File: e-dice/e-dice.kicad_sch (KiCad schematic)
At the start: 49 parts, among them J1 mid_conn_1, J2 top_conn_1, J3 mid_conn_2, J4 top_conn_2, J6 bot_conn_1, J7 bot_conn_2, J8 mid_conn_3, J9 mid_conn_4, Q1 2N3904, Q2 2N3904, Q3 2N3904, Q4 2N3906, Q5 2N3904, Q6 2N3904, Q7 2N3904, SW1 SW_SPDT, U1 4017

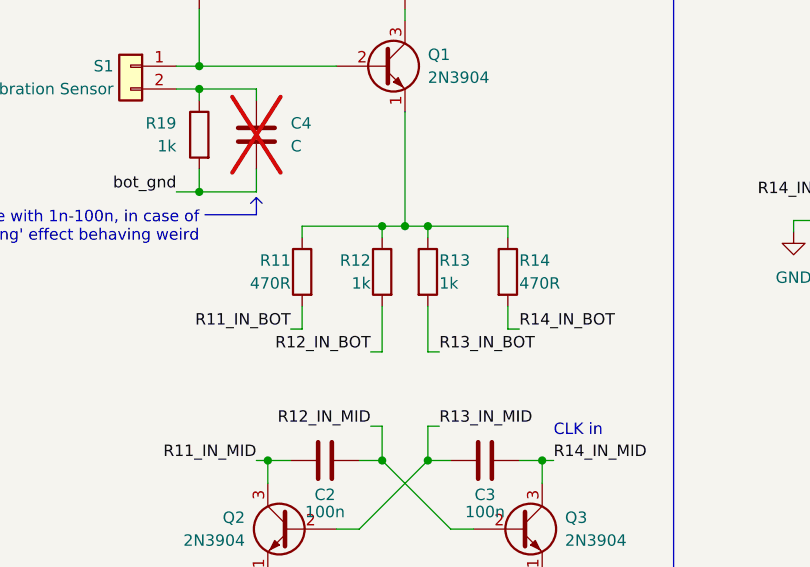
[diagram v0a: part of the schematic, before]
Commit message: Finished crossing for production, modified other
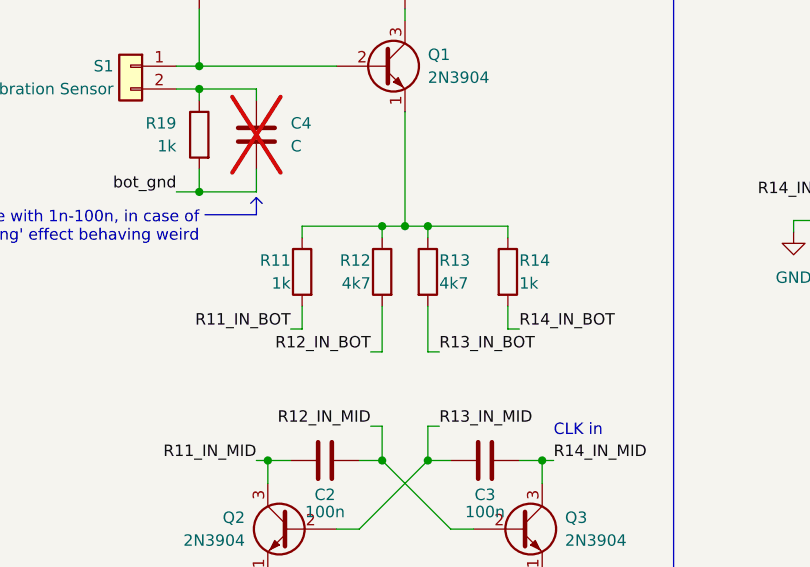
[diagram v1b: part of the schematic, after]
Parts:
- R11, R14: value 470R -> 1k
- R12, R13: value 1k -> 4k7
